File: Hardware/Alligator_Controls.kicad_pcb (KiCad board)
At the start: 2 copper layers, 60 x 110 mm, 25 parts, among them J1 Audio_In_L, J10 Feedback_CV, J11 Audio_In_R, J12 Audio_Out_R, J13 Audio_Out_L, J14 USB_B_Micro, J2 Delay_CV_L, J3 Conn_01x08_Female, J4 Conn_01x08_Female, J5 Conn_01x08_Female, J6 Conn_01x08_Female, J7 Mix_CV, J8 Delay_CV_R, J9 Clock

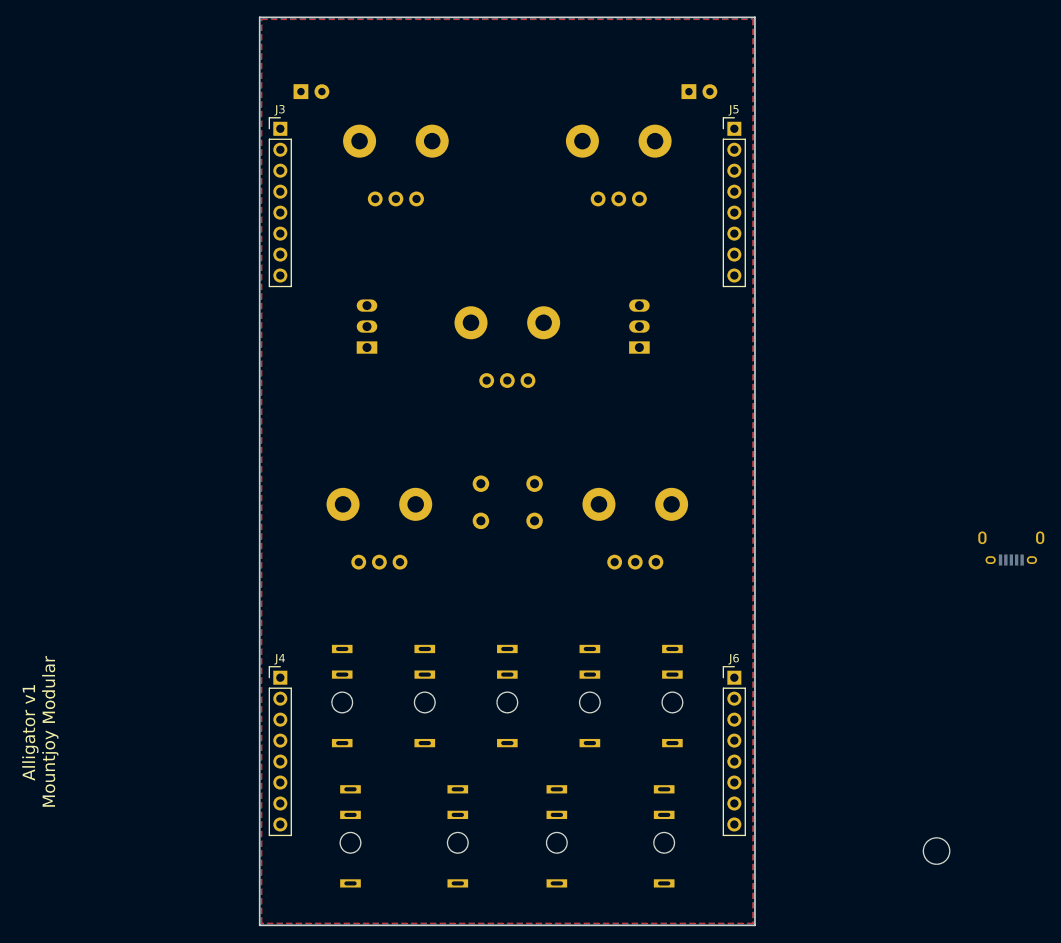
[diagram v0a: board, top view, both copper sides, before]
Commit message: Tooling holes added for SMT assembly; started routing control PCB
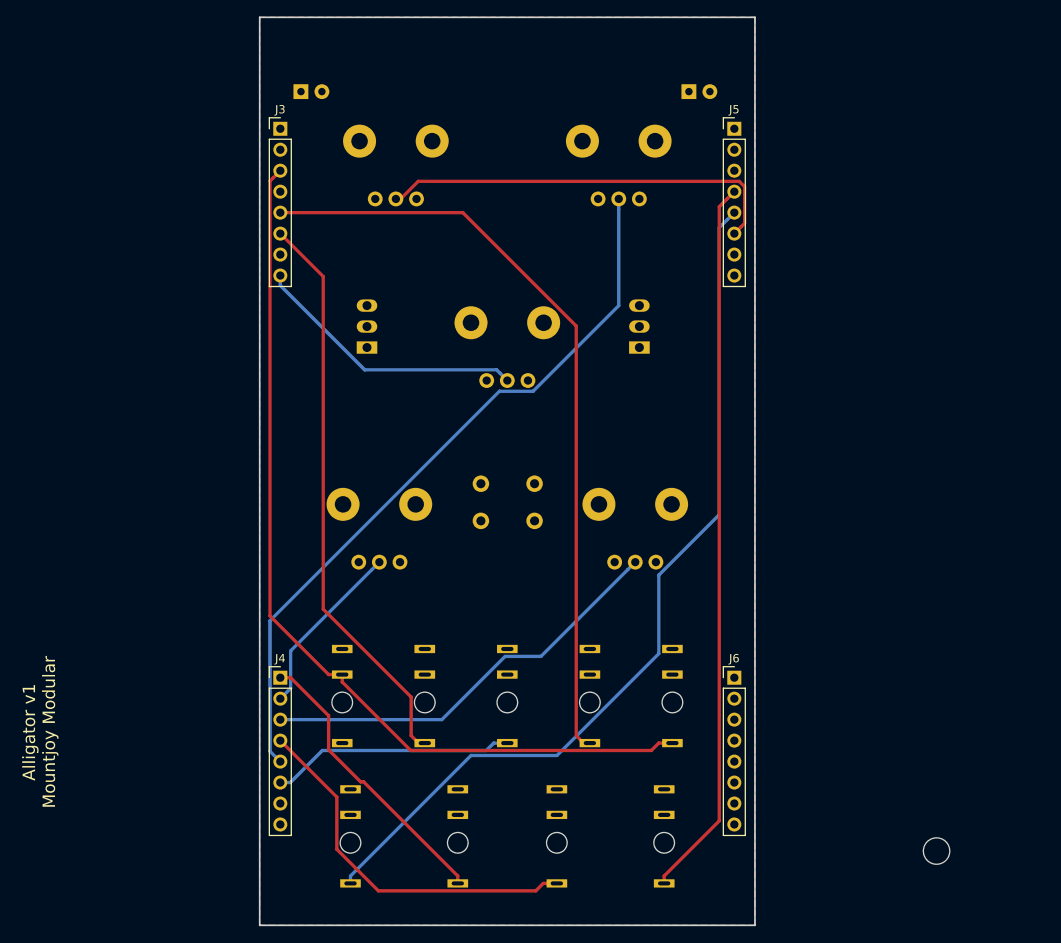
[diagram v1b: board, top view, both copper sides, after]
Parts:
- removed J14: USB_B_Micro, Connectors:USB_Micro-B
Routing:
- net /EXT_AUDIO_IN_L: track 0.00 -> 110.9 mm
- net /EXT_AUDIO_OUT_R: track 0.00 -> 106.6 mm
- net /DELAY_CV_L: track 0.00 -> 93.2 mm
- net /DELAY_POT_L: track 0.00 -> 88.6 mm
- net /EXT_AUDIO_OUT_L: track 0.00 -> 87.3 mm
- net /DELAY_CV_R: track 0.00 -> 69.4 mm
- net /FEEDBACK_POT: track 0.00 -> 50.9 mm
- net /DELAY_POT_R: track 0.00 -> 49.6 mm
- net /FEEDBACK_CV: track 0.00 -> 45.1 mm
- net /MIX_CV: track 0.00 -> 34.8 mm
- net /TONE_POT: track 0.00 -> 33.5 mm
- net /CLOCK: track 0.00 -> 29.5 mm
- net /MIX_POT: track 0.00 -> 21.5 mm

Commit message: More controls routing
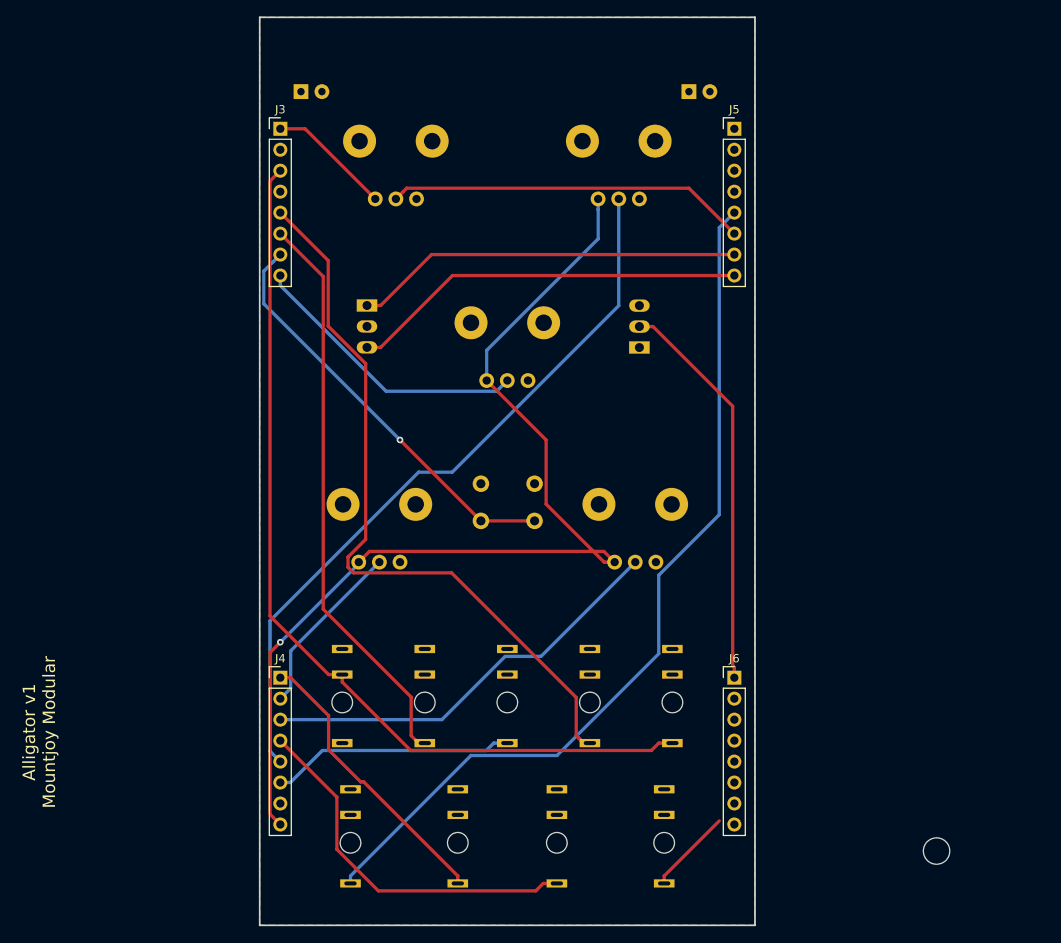
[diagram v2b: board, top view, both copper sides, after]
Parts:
- moved FXMODE1 5.09 mm to (113.0, 84.9), turned to 270 degrees
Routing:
- net +3.3VA: track 0.00 -> 140.6 mm, vias 0 -> 1
- net /EXT_AUDIO_OUT_L: track 87.3 -> 10.3 mm
- net /RESET: track 0.00 -> 50.5 mm, vias 0 -> 1
- net /DELAY_CHORUS: track 0.00 -> 48.3 mm
- net /MODE2: track 0.00 -> 48.1 mm
- net /MODE1: track 0.00 -> 47.1 mm
- net /DELAY_POT_R: track 49.6 -> 43.8 mm
- net /DELAY_CV_L: track 93.2 -> 90.2 mm
- net /TONE_POT: track 33.5 -> 34.5 mm

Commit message: Control PCB orientation tests
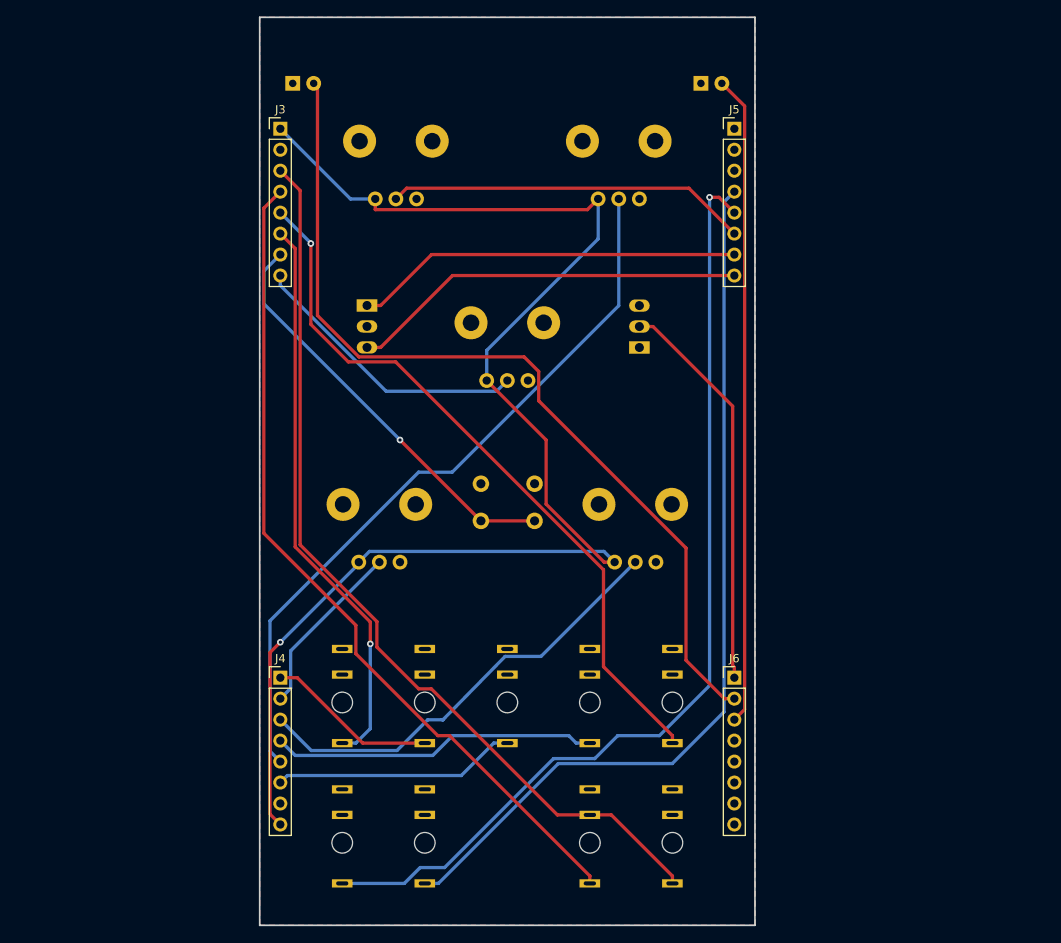
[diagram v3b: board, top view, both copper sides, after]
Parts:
- removed H1: MountingHole_Pad, Mounting_Holes:MountingHole_3.2mm_M3
- moved J11 34.5 mm to (140.0, 150.0)
- moved J13 29.0 mm to (120.0, 150.0)
- moved J10 17.5 mm to (140.0, 133.0)
- moved J7 17.5 mm to (120.0, 133.0)
- moved J1 17.0 mm to (150.0, 150.0)
- moved J2 10.0 mm to (150.0, 133.0)
- moved J8 10.0 mm to (110.0, 133.0)
- moved D1 1.76 mm to (153.4, 58.0)
- moved D2 1.41 mm to (104.0, 58.0)
- moved J12 1.00 mm to (110.0, 150.0)
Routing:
- net /LED2: track 0.00 -> 108.1 mm
- net /EXT_AUDIO_IN_R: track 0.00 -> 101.8 mm
- net /EXT_AUDIO_OUT_L: track 10.3 -> 108.4 mm
- net /LED1: track 0.00 -> 78.7 mm
- net +3.3VA: track 140.6 -> 169.4 mm
- net /MIX_CV: track 34.8 -> 20.8 mm
- net /EXT_AUDIO_OUT_R: track 106.6 -> 117.3 mm, vias 0 -> 1
- net /FEEDBACK_CV: track 45.1 -> 39.6 mm
- net /FEEDBACK_POT: track 50.9 -> 54.2 mm
- net /DELAY_CV_L: track 90.2 -> 87.3 mm, vias 0 -> 1
- net /DELAY_CV_R: track 69.4 -> 68.6 mm, vias 0 -> 1
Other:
- net class Default: trace_width 0.25 -> 0.4
- board text added: "Alligator Controls v1 Mountjoy Modular"
- board text removed: "Alligator v1 Mountjoy Modular"

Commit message: Completed first draft of Panel PCB
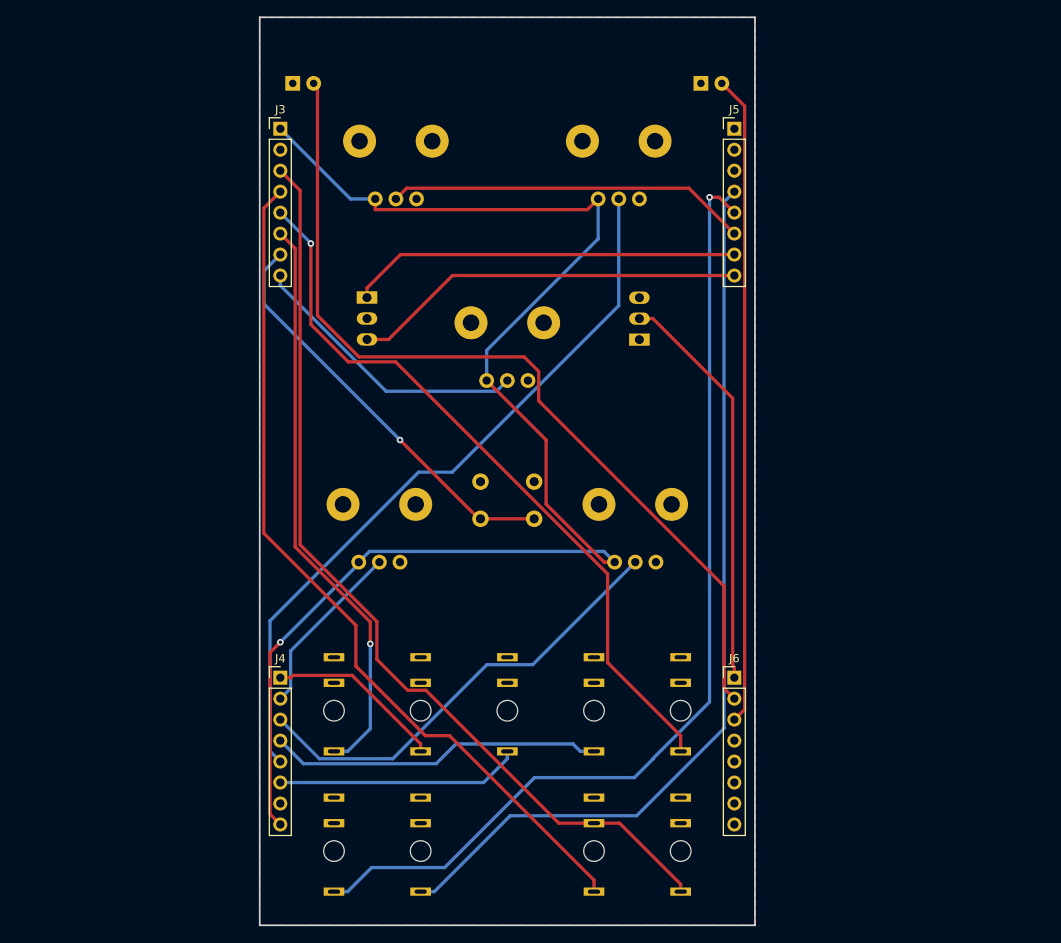
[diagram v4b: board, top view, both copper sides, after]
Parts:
- moved J1 1.41 mm to (151.0, 151.0)
- moved J12 1.41 mm to (109.0, 151.0)
- moved J2 1.41 mm to (151.0, 134.0)
- moved J8 1.41 mm to (109.0, 134.0)
- moved J10 1.12 mm to (140.5, 134.0)
- moved J11 1.12 mm to (140.5, 151.0)
- moved J13 1.12 mm to (119.5, 151.0)
- moved J7 1.12 mm to (119.5, 134.0)
- moved J9 1.00 mm to (130.0, 134.0)
- moved FXMODE1 0.96 mm to (113.0, 83.9)
- moved FXTYPE1 0.96 mm to (146.0, 89.0)
- moved RESET1 0.25 mm to (126.8, 110.8)
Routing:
- net /EXT_AUDIO_OUT_R: track 117.3 -> 120.0 mm
- net /EXT_AUDIO_IN_L: track 110.7 -> 113.0 mm
- net /EXT_AUDIO_OUT_L: track 108.4 -> 110.5 mm
- net /EXT_AUDIO_IN_R: track 101.8 -> 103.9 mm
- net /DELAY_CV_R: track 68.6 -> 70.0 mm
- net /DELAY_CV_L: track 87.3 -> 88.7 mm
- net /DELAY_CHORUS: track 48.3 -> 49.2 mm
- net /FEEDBACK_CV: track 39.6 -> 40.5 mm
- net /LED2: track 108.1 -> 107.4 mm
- net /MIX_CV: track 20.8 -> 21.5 mm
- net /FEEDBACK_POT: track 54.2 -> 54.8 mm
